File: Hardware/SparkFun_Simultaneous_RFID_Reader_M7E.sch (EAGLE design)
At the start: 41 parts, among them J5 U.FL, U1 UHF_RFID_NANO_MODULE_M7E_HECTO, U2 CH340C

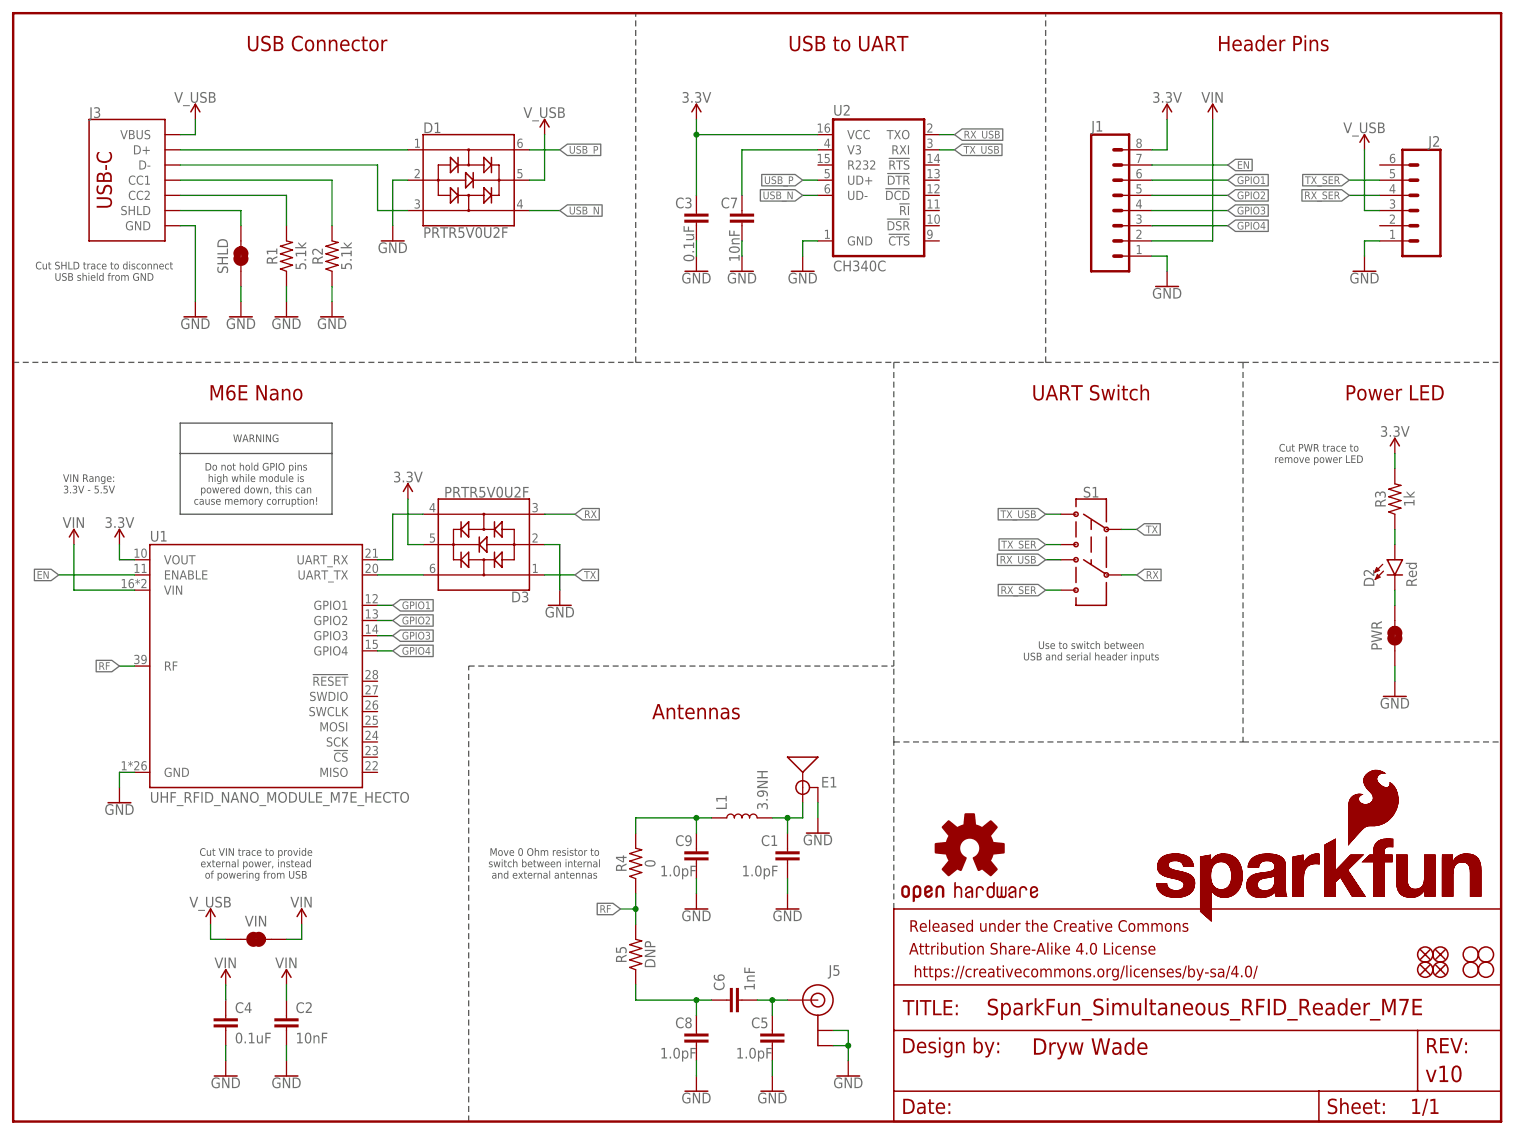
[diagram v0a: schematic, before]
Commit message: Change VIN selection jumper
Now uses a 3-way jumper to independently select USB, VCC from serial head, or just dedicated VIN pin
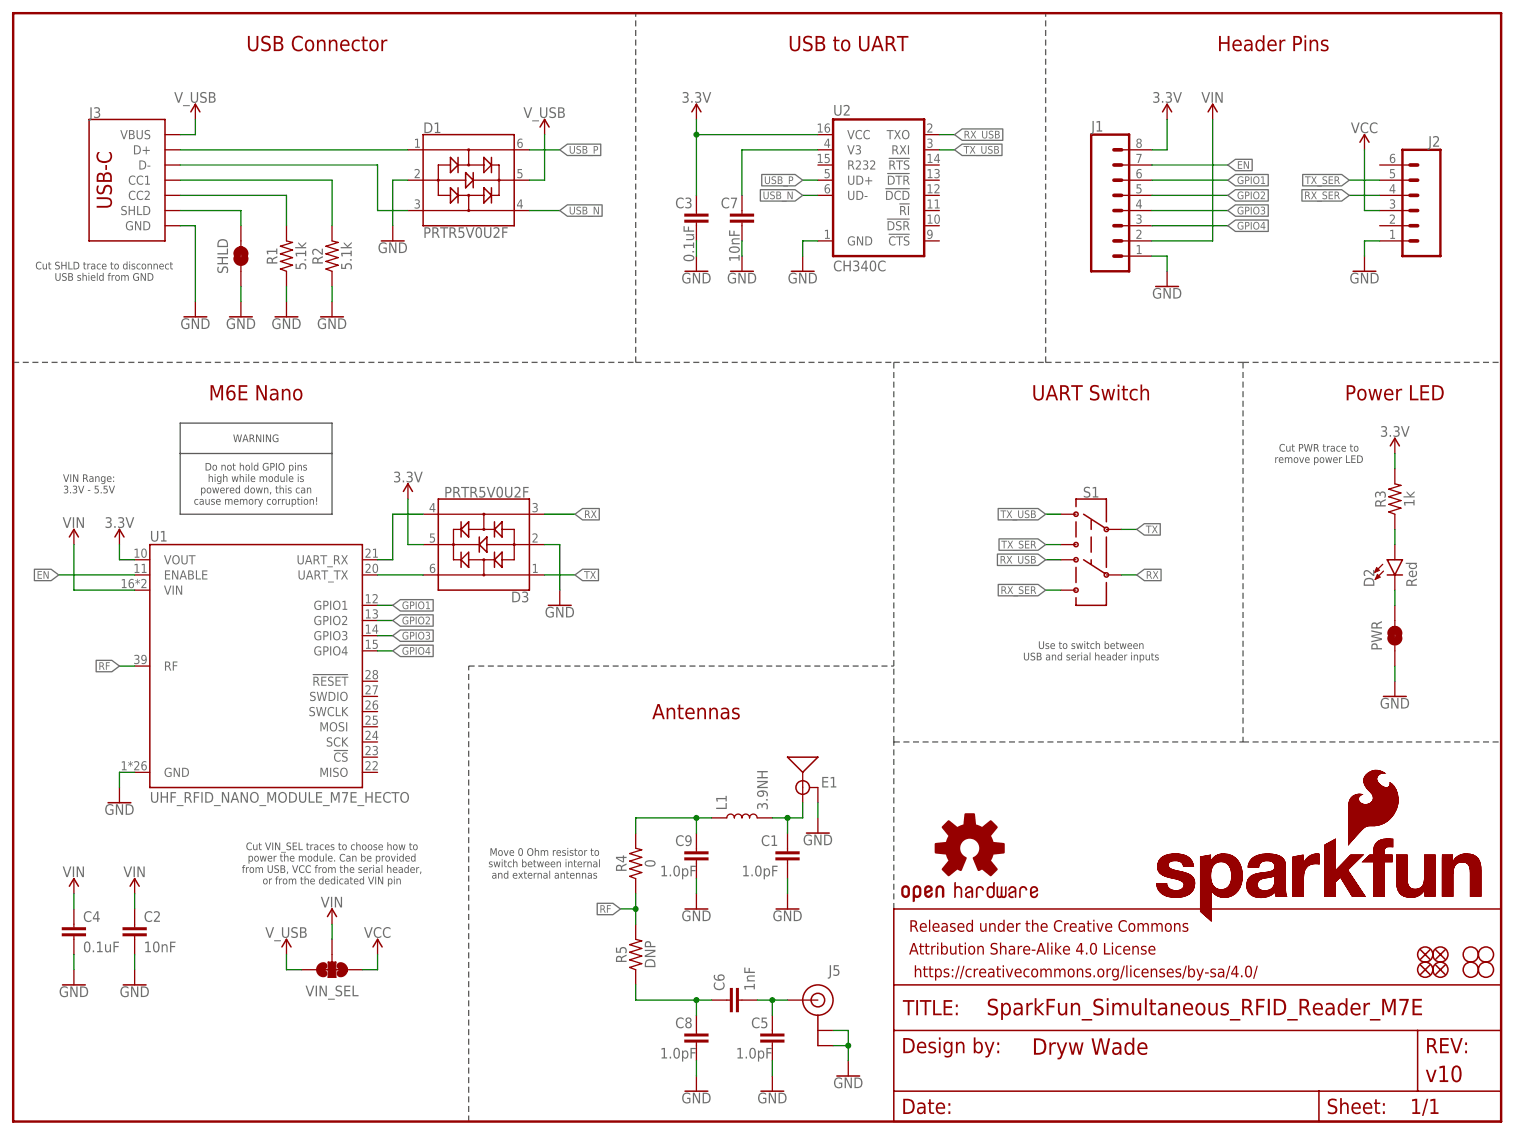
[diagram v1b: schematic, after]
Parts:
- removed VIN: JUMPER-SMT_2_NC_TRACE_SILK, SparkFun-Jumpers:JUMPER-SMT_2_NC_TRACE_SILK
- added VIN_SEL: JUMPER-SMT_3_2-NC_TRACE_SILK, SparkFun-Jumpers:JUMPER-SMT_3_2-NC_TRACE_SILK
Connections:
- new net VCC: J2.3, VIN_SEL.1
- net VIN: now also VIN_SEL.2; no longer VIN.2
- net V_USB: now also VIN_SEL.3; no longer J2.3, VIN.1
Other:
- note added: "Cut VIN_SEL traces to choose how to power the module. Can be provided from USB, VCC from the serial header, or from the dedicated VIN pin"
- note removed: "Cut VIN trace to provide external power, instead of powering from USB"
- moved on the sheet: C2, C4

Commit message: Change 3.3V net to VOUT
The M7E internal regulator actually outputs 2.5V when idle
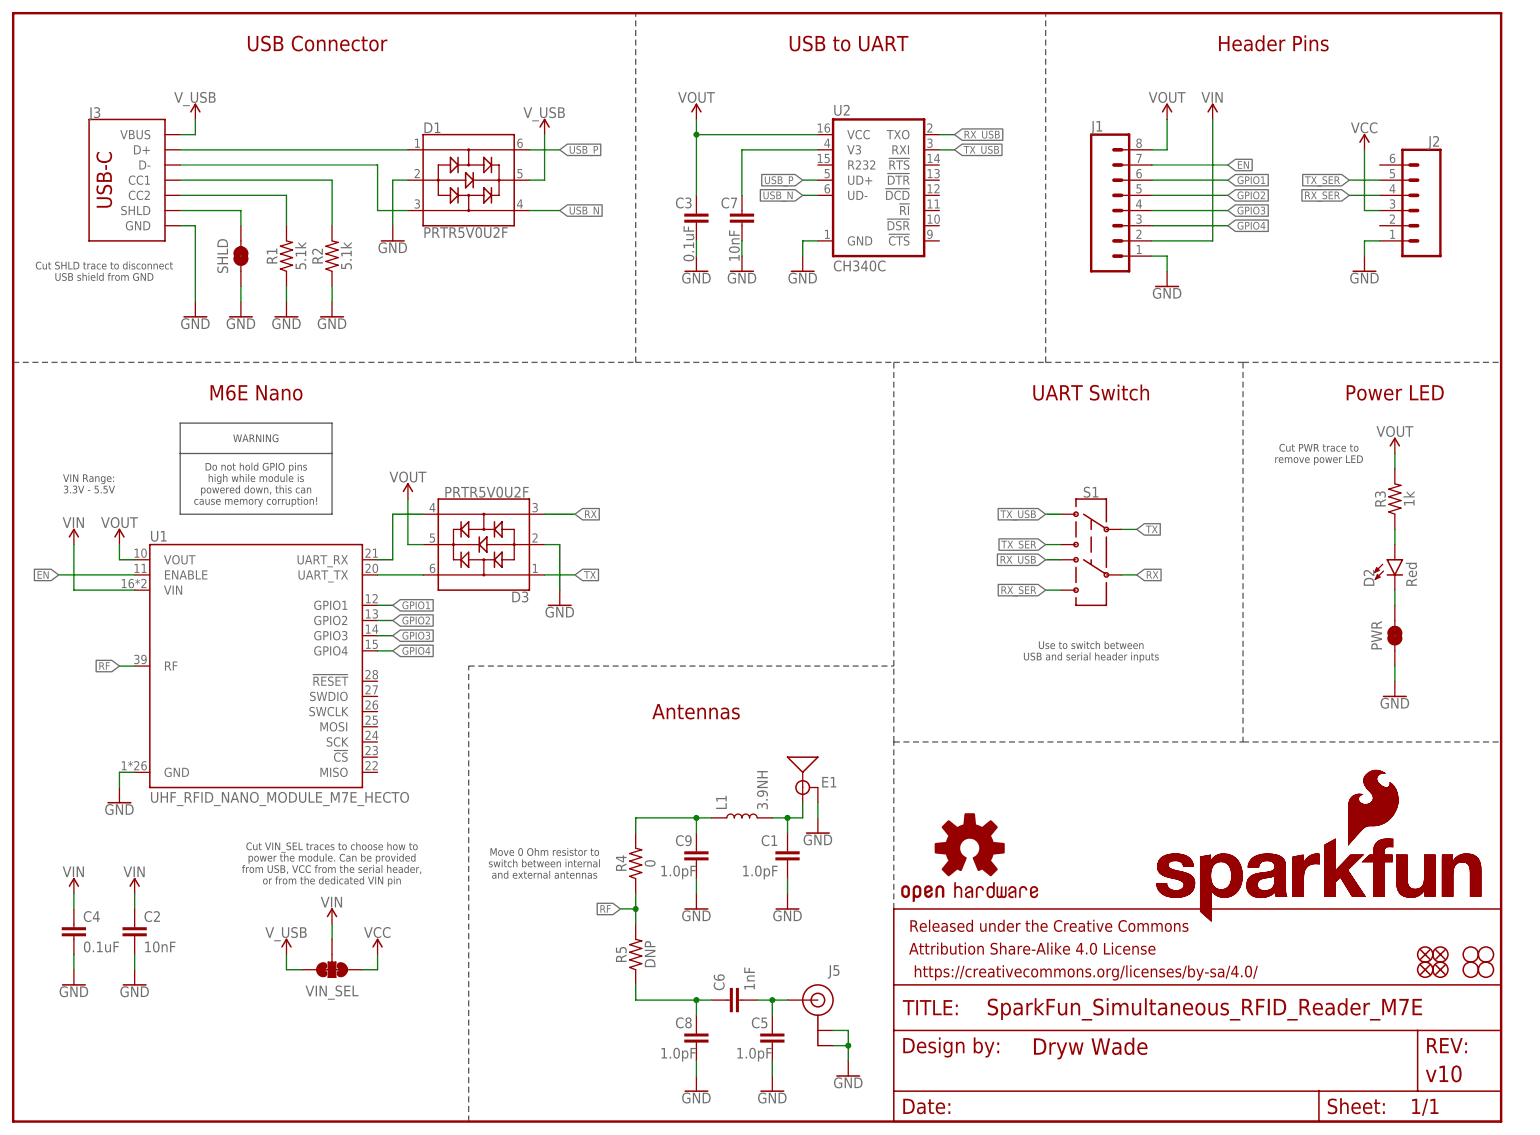
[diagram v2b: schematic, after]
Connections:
- net 3.3V renamed VOUT
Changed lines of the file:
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@@
 <part name="GND5" library="SparkFun-PowerSymbols" deviceset="GND" device=""/>
 <part name="SUPPLY1" library="SparkFun-PowerSymbols" deviceset="V_USB" device=""/>
-<part name="SUPPLY2" library="SparkFun-PowerSymbols" deviceset="3.3V" device=""/>
 <part name="SHLD" library="SparkFun-Jumpers" deviceset="JUMPER-SMT_2_NC_TRACE" device="_SILK" package3d_urn="urn:adsk.eagle:package:39281/1"/>
 <part name="GND6" library="SparkFun-PowerSymbols" deviceset="GND" device=""/>
@@
 <part name="GND9" library="SparkFun-PowerSymbols" deviceset="GND" device=""/>
 <part name="SUPPLY3" library="SparkFun-PowerSymbols" deviceset="V_USB" device=""/>
-<part name="SUPPLY4" library="SparkFun-PowerSymbols" deviceset="3.3V" device=""/>
 <part name="SUPPLY5" library="SparkFun-PowerSymbols" deviceset="VIN" device=""/>
 <part name="S1" library="SparkFun-Switches" deviceset="SWITCH-DPDT" device="-SMD-AYZ0202"/>
@@
 <part name="R3" library="SparkFun-Resistors" deviceset="1KOHM" device="-0603-1/10W-1%" value="1k"/>
 <part name="GND10" library="SparkFun-PowerSymbols" deviceset="GND" device=""/>
-<part name="SUPPLY8" library="SparkFun-PowerSymbols" deviceset="3.3V" device=""/>
 <part name="C2" library="SparkFun-Capacitors" deviceset="10NF" device="-0603-50V-10%" value="10nF"/>
 <part name="C3" library="SparkFun-Capacitors" deviceset="0.1UF" device="-0603-25V-(+80/-20%)" value="0.1uF"/>
@@
 <part name="GND14" library="SparkFun-PowerSymbols" deviceset="GND" device=""/>
 <part name="GND15" library="SparkFun-PowerSymbols" deviceset="GND" device=""/>
-<part name="SUPPLY12" library="SparkFun-PowerSymbols" deviceset="3.3V" device=""/>
 <part name="SUPPLY13" library="SparkFun-PowerSymbols" deviceset="VIN" device=""/>
 <part name="J5" library="SparkFun-Connectors" deviceset="U.FL" device="" value="U.FL"/>
@@
 <part name="D3" library="SparkFun-IC-Power" deviceset="PRTR5V0U2" device="F"/>
 <part name="GND19" library="SparkFun-PowerSymbols" deviceset="GND" device=""/>
-<part name="SUPPLY10" library="SparkFun-PowerSymbols" deviceset="3.3V" device=""/>
 <part name="J1" library="SparkFun-Connectors" deviceset="CONN_08" device="NO_SILK_DNP"/>
 <part name="J2" library="SparkFun-Connectors" deviceset="CONN_06" device="NO_SILK_NO_POP"/>
@@
 <part name="SUPPLY15" library="SparkFun-PowerSymbols" deviceset="VCC" device=""/>
 <part name="SUPPLY16" library="SparkFun-PowerSymbols" deviceset="VCC" device=""/>
+<part name="SUPPLY14" library="SparkFun-PowerSymbols" deviceset="VOUT" device=""/>
+<part name="SUPPLY4" library="SparkFun-PowerSymbols" deviceset="VOUT" device=""/>
+<part name="SUPPLY12" library="SparkFun-PowerSymbols" deviceset="VOUT" device=""/>
+<part name="SUPPLY2" library="SparkFun-PowerSymbols" deviceset="VOUT" device=""/>
+<part name="SUPPLY10" library="SparkFun-PowerSymbols" deviceset="VOUT" device=""/>
 </parts>
 <sheets>
@@
 <attribute name="VALUE" x="30.48" y="170.434" size="1.778" layer="96" align="bottom-center"/>
 </instance>
-<instance part="SUPPLY2" gate="G$1" x="114.3" y="167.64" smashed="yes">
-<attribute name="VALUE" x="114.3" y="170.434" size="1.778" layer="96" align="bottom-center"/>
-</instance>
 <instance part="SHLD" gate="G$1" x="38.1" y="144.78" smashed="yes" rot="R90">
 <attribute name="NAME" x="35.052" y="144.78" size="1.778" layer="95" font="vector" rot="R90" align="center"/>
@@
 <instance part="SUPPLY3" gate="G$1" x="88.9" y="165.1" smashed="yes">
 <attribute name="VALUE" x="88.9" y="167.894" size="1.778" layer="96" align="bottom-center"/>
-</instance>
-<instance part="SUPPLY4" gate="G$1" x="17.78" y="96.52" smashed="yes">
-<attribute name="VALUE" x="17.78" y="99.314" size="1.778" layer="96" align="bottom-center"/>
 </instance>
 <instance part="SUPPLY5" gate="G$1" x="10.16" y="96.52" smashed="yes">
@@
 <attribute name="VALUE" x="231.14" y="70.866" size="1.778" layer="96" align="top-center"/>
 </instance>
-<instance part="SUPPLY8" gate="G$1" x="231.14" y="111.76" smashed="yes">
-<attribute name="VALUE" x="231.14" y="114.554" size="1.778" layer="96" align="bottom-center"/>
-</instance>
 <instance part="C2" gate="G$1" x="20.32" y="30.48" smashed="yes">
 <attribute name="NAME" x="21.844" y="33.401" size="1.778" layer="95" font="vector"/>
@@
 <attribute name="VALUE" x="226.06" y="141.986" size="1.778" layer="96" align="top-center"/>
 </instance>
-<instance part="SUPPLY12" gate="G$1" x="193.04" y="167.64" smashed="yes">
-<attribute name="VALUE" x="193.04" y="170.434" size="1.778" layer="96" align="bottom-center"/>
-</instance>
 <instance part="SUPPLY13" gate="G$1" x="200.66" y="167.64" smashed="yes">
 <attribute name="VALUE" x="200.66" y="170.434" size="1.778" layer="96" align="bottom-center"/>
@@
 <attribute name="VALUE" x="91.44" y="86.106" size="1.778" layer="96" align="top-center"/>
 </instance>
-<instance part="SUPPLY10" gate="G$1" x="66.04" y="104.14" smashed="yes">
-<attribute name="VALUE" x="66.04" y="106.934" size="1.778" layer="96" align="bottom-center"/>
-</instance>
 <instance part="J1" gate="G$1" x="185.42" y="152.4" smashed="yes">
 <attribute name="VALUE" x="180.34" y="139.954" size="1.778" layer="96" font="vector"/>
@@
 <instance part="SUPPLY16" gate="G$1" x="226.06" y="162.56" smashed="yes">
 <attribute name="VALUE" x="226.06" y="165.354" size="1.778" layer="96" font="vector" align="bottom-center"/>
+</instance>
+<instance part="SUPPLY14" gate="G$1" x="17.78" y="96.52" smashed="yes">
+<attribute name="VALUE" x="17.78" y="99.314" size="1.778" layer="96" font="vector" align="bottom-center"/>
+</instance>
+<instance part="SUPPLY4" gate="G$1" x="193.04" y="167.64" smashed="yes">
+<attribute name="VALUE" x="193.04" y="170.434" size="1.778" layer="96" font="vector" align="bottom-center"/>
+</instance>
+<instance part="SUPPLY12" gate="G$1" x="114.3" y="167.64" smashed="yes">
+<attribute name="VALUE" x="114.3" y="170.434" size="1.778" layer="96" font="vector" align="bottom-center"/>
+</instance>
+<instance part="SUPPLY2" gate="G$1" x="66.04" y="104.14" smashed="yes">
+<attribute name="VALUE" x="66.04" y="106.934" size="1.778" layer="96" font="vector" align="bottom-center"/>
+</instance>
+<instance part="SUPPLY10" gate="G$1" x="231.14" y="111.76" smashed="yes">
+<attribute name="VALUE" x="231.14" y="114.554" size="1.778" layer="96" font="vector" align="bottom-center"/>
 </instance>
 </instances>
@@
 </segment>
 </net>
-<net name="3.3V" class="0">
-<segment>
-<pinref part="U2" gate="U1" pin="VCC"/>
-<wire x1="134.62" y1="165.1" x2="114.3" y2="165.1" width="0.1524" layer="91"/>
-<pinref part="SUPPLY2" gate="G$1" pin="3.3V"/>
-<wire x1="114.3" y1="165.1" x2="114.3" y2="167.64" width="0.1524" layer="91"/>
-<pinref part="C3" gate="G$1" pin="1"/>
-<wire x1="114.3" y1="154.94" x2="114.3" y2="165.1" width="0.1524" layer="91"/>
-<junction x="114.3" y="165.1"/>
-</segment>
-<segment>
-<pinref part="U1" gate="U1" pin="VOUT"/>
-<wire x1="20.32" y1="93.98" x2="17.78" y2="93.98" width="0.1524" layer="91"/>
-<wire x1="17.78" y1="93.98" x2="17.78" y2="96.52" width="0.1524" layer="91"/>
-<pinref part="SUPPLY4" gate="G$1" pin="3.3V"/>
-</segment>
-<segment>
-<wire x1="190.5" y1="162.56" x2="193.04" y2="162.56" width="0.1524" layer="91"/>
-<wire x1="193.04" y1="162.56" x2="193.04" y2="167.64" width="0.1524" layer="91"/>
-<pinref part="SUPPLY12" gate="G$1" pin="3.3V"/>
-<pinref part="J1" gate="G$1" pin="8"/>
-</segment>
-<segment>
-<pinref part="D3" gate="D1" pin="5"/>
-<wire x1="68.58" y1="96.52" x2="66.04" y2="96.52" width="0.1524" layer="91"/>
-<wire x1="66.04" y1="96.52" x2="66.04" y2="104.14" width="0.1524" layer="91"/>
-<pinref part="SUPPLY10" gate="G$1" pin="3.3V"/>
-</segment>
-<segment>
-<pinref part="R3" gate="G$1" pin="2"/>
-<pinref part="SUPPLY8" gate="G$1" pin="3.3V"/>
-<wire x1="231.14" y1="109.22" x2="231.14" y2="111.76" width="0.1524" layer="91"/>
-</segment>
-</net>
 <net name="SHLD" class="0">
 <segment>
@@
 </segment>
 </net>
+<net name="VOUT" class="0">
+<segment>
+<pinref part="U1" gate="U1" pin="VOUT"/>
+<wire x1="20.32" y1="93.98" x2="17.78" y2="93.98" width="0.1524" layer="91"/>
+<wire x1="17.78" y1="93.98" x2="17.78" y2="96.52" width="0.1524" layer="91"/>
+<pinref part="SUPPLY14" gate="G$1" pin="VOUT"/>
+</segment>
+<segment>
+<wire x1="190.5" y1="162.56" x2="193.04" y2="162.56" width="0.1524" layer="91"/>
+<wire x1="193.04" y1="162.56" x2="193.04" y2="167.64" width="0.1524" layer="91"/>
+<pinref part="J1" gate="G$1" pin="8"/>
+<pinref part="SUPPLY4" gate="G$1" pin="VOUT"/>
+</segment>
+<segment>
+<pinref part="U2" gate="U1" pin="VCC"/>
+<wire x1="134.62" y1="165.1" x2="114.3" y2="165.1" width="0.1524" layer="91"/>
+<wire x1="114.3" y1="165.1" x2="114.3" y2="167.64" width="0.1524" layer="91"/>
+<pinref part="C3" gate="G$1" pin="1"/>
+<wire x1="114.3" y1="154.94" x2="114.3" y2="165.1" width="0.1524" layer="91"/>
+<junction x="114.3" y="165.1"/>
+<pinref part="SUPPLY12" gate="G$1" pin="VOUT"/>
+</segment>
+<segment>
+<pinref part="D3" gate="D1" pin="5"/>
+<wire x1="68.58" y1="96.52" x2="66.04" y2="96.52" width="0.1524" layer="91"/>
+<wire x1="66.04" y1="96.52" x2="66.04" y2="104.14" width="0.1524" layer="91"/>
+<pinref part="SUPPLY2" gate="G$1" pin="VOUT"/>
+</segment>
+<segment>
+<pinref part="R3" gate="G$1" pin="2"/>
+<wire x1="231.14" y1="109.22" x2="231.14" y2="111.76" width="0.1524" layer="91"/>
+<pinref part="SUPPLY10" gate="G$1" pin="VOUT"/>
+</segment>
+</net>
